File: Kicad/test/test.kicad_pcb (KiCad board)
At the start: 4 copper layers, 46.8 x 47.5 mm, 74 parts, among them J1 SPKOUT, J2 Tag Con, P1 USB_C_Plug_USB2.0, SW1 SW_Push, SW2 SW_Push, SW4 SW_Push, SW5 SW_Push, U1 MAX98357A, U2 ESP32-S3-WROOM-1, U3 OV5640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

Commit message: Routing completed
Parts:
- C11, C12: moved to B.Cu
- moved C11 5.54 mm to (102.7, 56.4), turned to 0 degrees
- moved C12 4.62 mm to (102.7, 57.4), turned to 0 degrees
- moved NC1 0.32 mm to (102.7, 53.1)
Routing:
- net +2V8: track 20.4 -> 9.15 mm, vias 4 -> 1
- net SW_L1: track 34.8 -> 25.8 mm, vias 3 -> 1
- net CAM_Y8: track 18.5 -> 25.7 mm
- net GND: track 84.8 -> 78.9 mm, vias 58 -> 57
- net VSYS: track 114.4 -> 109.0 mm
- net CAM_Y7: track 18.7 -> 23.3 mm
- net CAM_PCLK: track 20.8 -> 25.5 mm
- net CAM_Y9: track 20.1 -> 23.4 mm
- net +3V3: track 140.5 -> 143.3 mm
- net CAM_MCLK: track 13.4 -> 16.1 mm
- net CAM_Y5: track 21.4 -> 23.9 mm
- net CAM_Y6: track 22.0 -> 23.7 mm
- net CAM_Y2: track 21.8 -> 23.4 mm
- net CAM_RESET: track 50.9 -> 49.4 mm
- net CAM_Y3: track 24.8 -> 23.4 mm
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- added copper zone on In2.Cu, net GND
- removed copper zone on In2.Cu, net +3V3
- removed copper zone on In2.Cu, net VSYS

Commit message: Routing Completed
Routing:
- net GND: track 78.9 -> 79.8 mm, vias 57 -> 56
- net VSYS: track 109.0 -> 109.6 mm
- net GPIO0: track 28.8 -> 28.3 mm

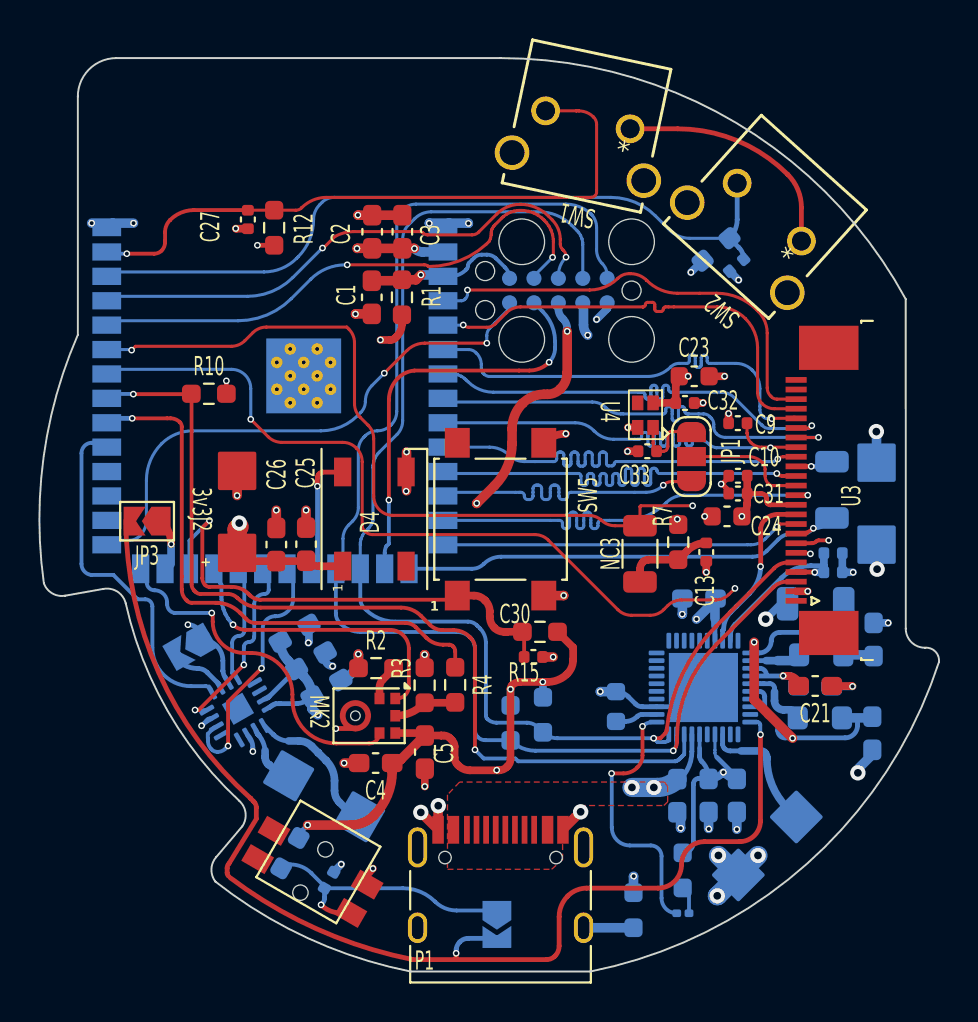
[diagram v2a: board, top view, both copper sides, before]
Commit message: Mounting Hole added
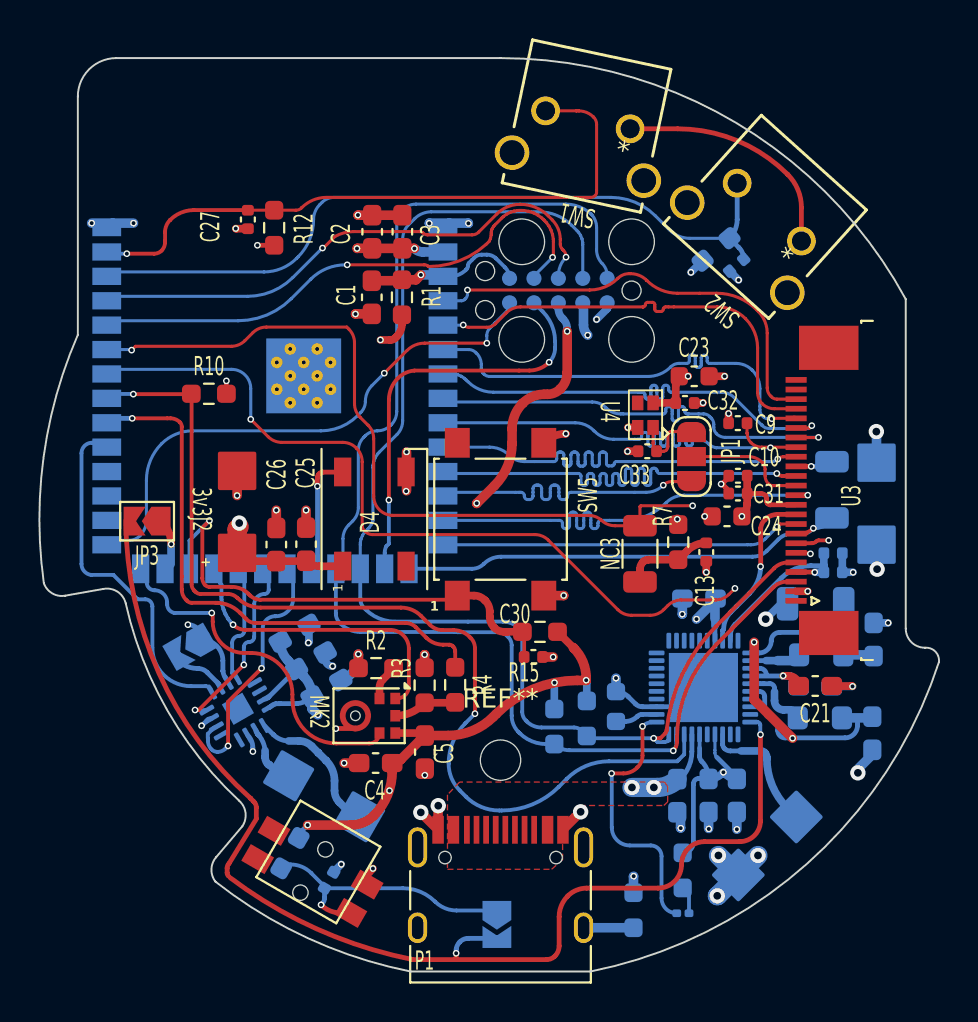
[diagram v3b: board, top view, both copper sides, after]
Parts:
- added REF**: MountingHole_2.1mm, MountingHole:MountingHole_2.1mm, F.Cu at (85.4, 67.2)
- moved R9 2.29 mm to (88.2, 65.4)
- moved R8 2.29 mm to (89.9, 65.0)
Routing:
- net PMIC_IRQ: track 47.7 -> 51.9 mm
- net +3V3: track 143.3 -> 146.1 mm
- net VSYS: track 109.6 -> 108.5 mm
- net GND: track 79.8 -> 79.1 mm
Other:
- board text removed: "Battery"

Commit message: Optimizing for DFM still pending
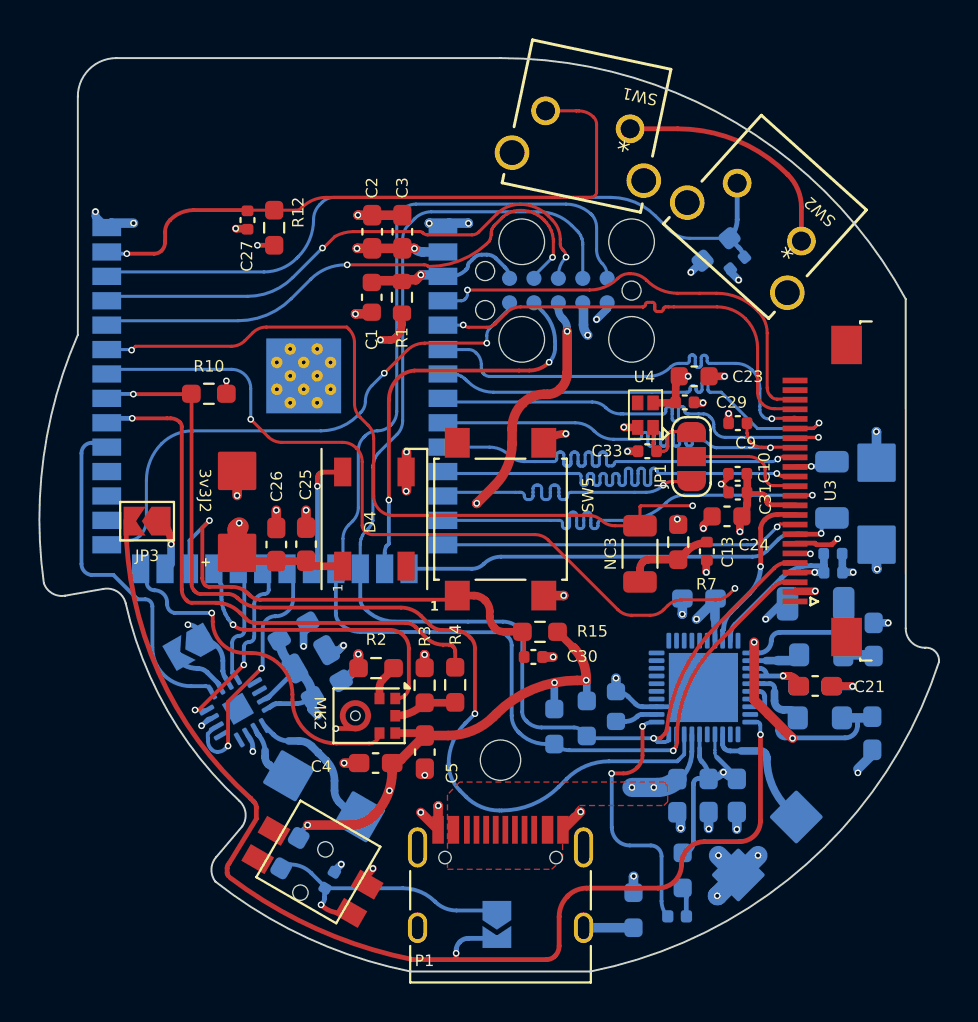
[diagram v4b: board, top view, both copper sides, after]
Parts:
- removed C32: 100n, Capacitor_SMD:C_0402_1005Metric
- added C34: 100n, Capacitor_SMD:C_0402_1005Metric, B.Cu at (76.5, 73.4)
- C1: footprint Capacitor_SMD:C_0603_1608Metric_Pad1.08x0.95mm_HandSolder -> Capacitor_SMD:C_0603_1608Metric
- C29: moved to F.Cu
- C8: footprint Capacitor_SMD:C_0603_1608Metric_Pad1.08x0.95mm_HandSolder -> Capacitor_SMD:C_0805_2012Metric
- D1: footprint LED_SMD:LED_0201_0603Metric -> LED_SMD:LED_0402_1005Metric
- R1: footprint Resistor_SMD:R_0603_1608Metric_Pad0.98x0.95mm_HandSolder -> Resistor_SMD:R_0603_1608Metric
- moved C28 38.5 mm to (97.7, 41.3), turned to -140 degrees
- moved C29 7.63 mm to (95.0, 48.6), turned to 0 degrees
- moved U3 2.06 mm to (100.1, 53.2)
- moved D1 0.34 mm to (94.6, 75.3)
- moved C6 0.12 mm to (74.6, 60.5)
- moved C10 0.10 mm to (97.7, 52.3)
- moved C8 0.08 mm to (75.5, 61.9)
- moved C13 0.05 mm to (96.1, 56.3)
- moved C31 0.05 mm to (97.8, 53.2), turned to 180 degrees
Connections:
- C28 pad 1: Net-(JP2-A) -> SW_L2
- C29 pad 1: SW_L2 -> +3V3CAM
- C31 pad 1: GND -> +3V3CAM
- C31 pad 2: +3V3CAM -> GND
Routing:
- net GND: track 79.1 -> 80.9 mm
- net +3V3CAM: track 43.4 -> 44.6 mm
- net CAM_VSYNC: track 51.4 -> 52.3 mm
- net CAM_PWDN: track 24.4 -> 23.7 mm
- net Net-(D1-A): track 1.49 -> 2.03 mm

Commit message: DFM completed Logo added
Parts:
- added G***: LOGO, LOGO, B.Cu at (95.1, 54.6)
- added G***: LOGO, LOGO, B.Cu at (86.3, 54.7)
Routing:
- net CAM_PWDN: track 23.7 -> 24.7 mm
- net GND: track 80.9 -> 81.2 mm, vias 56 -> 83
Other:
- board text added: "BAT"
- board text added: "Date"
- board text added: "Designed by"
- board text added: "Power"
- board text added: "Rev."
- board text added: "Speaker"
- board text added: "Test"
- board text added: "USB"
